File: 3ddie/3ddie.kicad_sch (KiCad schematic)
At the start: 53 parts, among them J1 USB4105-GF-A, J2 TRS_MIDI_IN, J3 TRS_MIDI_OUT, U1 W25Q128JV, U2 RP2040, U3 MCP1702T-3302E_CB, U4 MGC3130-I/MQ, U5 MCP1416R, U6 6N137, U7 BoostedElectrodes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

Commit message: continue adding footprints
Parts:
- C16, C17: footprint Capacitor_SMD:C_0603_1608Metric -> Capacitor_SMD:C_0402_1005Metric
- J2, J3: footprint (none) -> Connector_Audio:Jack_3.5mm_CUI_SJ-3523-SMT_Horizontal; Digikey Catalog # (none) -> CP-3523SJCT-ND; Manufacturer Part # (none) -> SJ-3523-SMT-TR
- U4: footprint (none) -> 3ddie:MGC3130T-I_MQ
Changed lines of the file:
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@@
       (effects (font (size 1.27 1.27)) (justify right))
     )
-    (property "Footprint" "Capacitor_SMD:C_0603_1608Metric" (id 2) (at 259.3848 152.4 0)
+    (property "Footprint" "Capacitor_SMD:C_0402_1005Metric" (id 2) (at 259.3848 152.4 0)
       (effects (font (size 1.27 1.27)) hide)
     )
@@
       (effects (font (size 1.27 1.27)) (justify right))
     )
-    (property "Footprint" "" (id 2) (at 207.645 201.93 0)
-      (effects (font (size 1.27 1.27)) hide)
-    )
-    (property "Datasheet" "~" (id 3) (at 207.645 201.93 0)
+    (property "Footprint" "Connector_Audio:Jack_3.5mm_CUI_SJ-3523-SMT_Horizontal" (id 2) (at 207.645 201.93 0)
+      (effects (font (size 1.27 1.27)) hide)
+    )
+    (property "Datasheet" "https://www.cuidevices.com/product/resource/sj-352x-smt.pdf" (id 3) (at 207.645 201.93 0)
+      (effects (font (size 1.27 1.27)) hide)
+    )
+    (property "Digikey Catalog #" "CP-3523SJCT-ND" (id 4) (at 207.645 201.93 0)
+      (effects (font (size 1.27 1.27)) hide)
+    )
+    (property "Manufacturer Part #" "SJ-3523-SMT-TR" (id 5) (at 207.645 201.93 0)
       (effects (font (size 1.27 1.27)) hide)
     )
@@
     (property "Reference" "J2" (id 0) (at 204.47 172.8302 0))
     (property "Value" "TRS_MIDI_IN" (id 1) (at 204.47 175.3671 0))
-    (property "Footprint" "" (id 2) (at 206.375 180.34 0)
-      (effects (font (size 1.27 1.27)) hide)
-    )
-    (property "Datasheet" "~" (id 3) (at 206.375 180.34 0)
+    (property "Footprint" "Connector_Audio:Jack_3.5mm_CUI_SJ-3523-SMT_Horizontal" (id 2) (at 206.375 180.34 0)
+      (effects (font (size 1.27 1.27)) hide)
+    )
+    (property "Datasheet" "https://www.cuidevices.com/product/resource/sj-352x-smt.pdf" (id 3) (at 206.375 180.34 0)
+      (effects (font (size 1.27 1.27)) hide)
+    )
+    (property "Digikey Catalog #" "CP-3523SJCT-ND" (id 4) (at 206.375 180.34 0)
+      (effects (font (size 1.27 1.27)) hide)
+    )
+    (property "Manufacturer Part #" "SJ-3523-SMT-TR" (id 5) (at 206.375 180.34 0)
       (effects (font (size 1.27 1.27)) hide)
     )
@@
       (effects (font (size 1.524 1.524)) (justify right))
     )
-    (property "Footprint" "" (id 2) (at 223.52 124.714 0)
+    (property "Footprint" "3ddie:MGC3130T-I_MQ" (id 2) (at 223.52 124.714 0)
       (effects (font (size 1.524 1.524)) hide)
     )
@@
       (effects (font (size 1.27 1.27)) (justify right))
     )
-    (property "Footprint" "Capacitor_SMD:C_0603_1608Metric" (id 2) (at 254.3048 152.4 0)
+    (property "Footprint" "Capacitor_SMD:C_0402_1005Metric" (id 2) (at 254.3048 152.4 0)
       (effects (font (size 1.27 1.27)) hide)
     )
@@
       (effects (font (size 1.524 1.524)))
     )
-    (property "Footprint" "" (id 2) (at 251.46 71.374 0)
+    (property "Footprint" "3ddie:MGC3130T-I_MQ" (id 2) (at 251.46 71.374 0)
       (effects (font (size 1.524 1.524)) hide)
     )
@@
     )
     (path "/900c03b9-9a9a-4efc-b87d-5814d26cd06f"
-      (reference "C16") (unit 1) (value "4.7μF") (footprint "Capacitor_SMD:C_0603_1608Metric")
+      (reference "C16") (unit 1) (value "4.7μF") (footprint "Capacitor_SMD:C_0402_1005Metric")
     )
     (path "/1a86f12e-e638-446c-972e-a7709025dbe9"
-      (reference "C17") (unit 1) (value "4.7μF") (footprint "Capacitor_SMD:C_0603_1608Metric")
+      (reference "C17") (unit 1) (value "4.7μF") (footprint "Capacitor_SMD:C_0402_1005Metric")
     )
     (path "/951f6575-df68-4f23-a749-6a530106a298"
@@
     )
     (path "/3f49297e-868a-4cfd-a836-aea36d28a6f3"
-      (reference "J2") (unit 1) (value "TRS_MIDI_IN") (footprint "")
+      (reference "J2") (unit 1) (value "TRS_MIDI_IN") (footprint "Connector_Audio:Jack_3.5mm_CUI_SJ-3523-SMT_Horizontal")
     )
     (path "/36954f5c-ded0-4f77-a0ed-a1fcda0fcb0f"
-      (reference "J3") (unit 1) (value "TRS_MIDI_OUT") (footprint "")
+      (reference "J3") (unit 1) (value "TRS_MIDI_OUT") (footprint "Connector_Audio:Jack_3.5mm_CUI_SJ-3523-SMT_Horizontal")
     )
     (path "/7ca43cf0-22a3-4ee0-a8c6-940bc048e7d1"
@@
     )
     (path "/a9329e99-609f-4c39-a02d-48cc774ada87"
-      (reference "U4") (unit 1) (value "MGC3130-I/MQ") (footprint "")
+      (reference "U4") (unit 1) (value "MGC3130-I/MQ") (footprint "3ddie:MGC3130T-I_MQ")
     )
     (path "/5936d240-6102-4439-994a-788eb8b3c026"
-      (reference "U4") (unit 2) (value "MGC3130-I/MQ") (footprint "")
+      (reference "U4") (unit 2) (value "MGC3130-I/MQ") (footprint "3ddie:MGC3130T-I_MQ")
     )
     (path "/15b2a124-1eb8-4d1a-932b-488f6e69f5b6"

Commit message: finish assigning footprints (other than electrodes)
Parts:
- U6: footprint (none) -> 3ddie:6N137_Leadbend
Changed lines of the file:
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@@
     (property "Reference" "U6" (id 0) (at 235.585 169.0202 0))
     (property "Value" "6N137" (id 1) (at 235.585 171.5571 0))
-    (property "Footprint" "" (id 2) (at 235.585 193.04 0)
+    (property "Footprint" "3ddie:6N137_Leadbend" (id 2) (at 235.585 193.04 0)
       (effects (font (size 1.27 1.27)) hide)
     )
@@
     )
     (path "/bca2ac86-8d9c-4b32-ab1d-2258827622a1"
-      (reference "U6") (unit 1) (value "6N137") (footprint "")
+      (reference "U6") (unit 1) (value "6N137") (footprint "3ddie:6N137_Leadbend")
     )
     (path "/0030390e-c97e-47e6-97d2-f7c983a931fc"

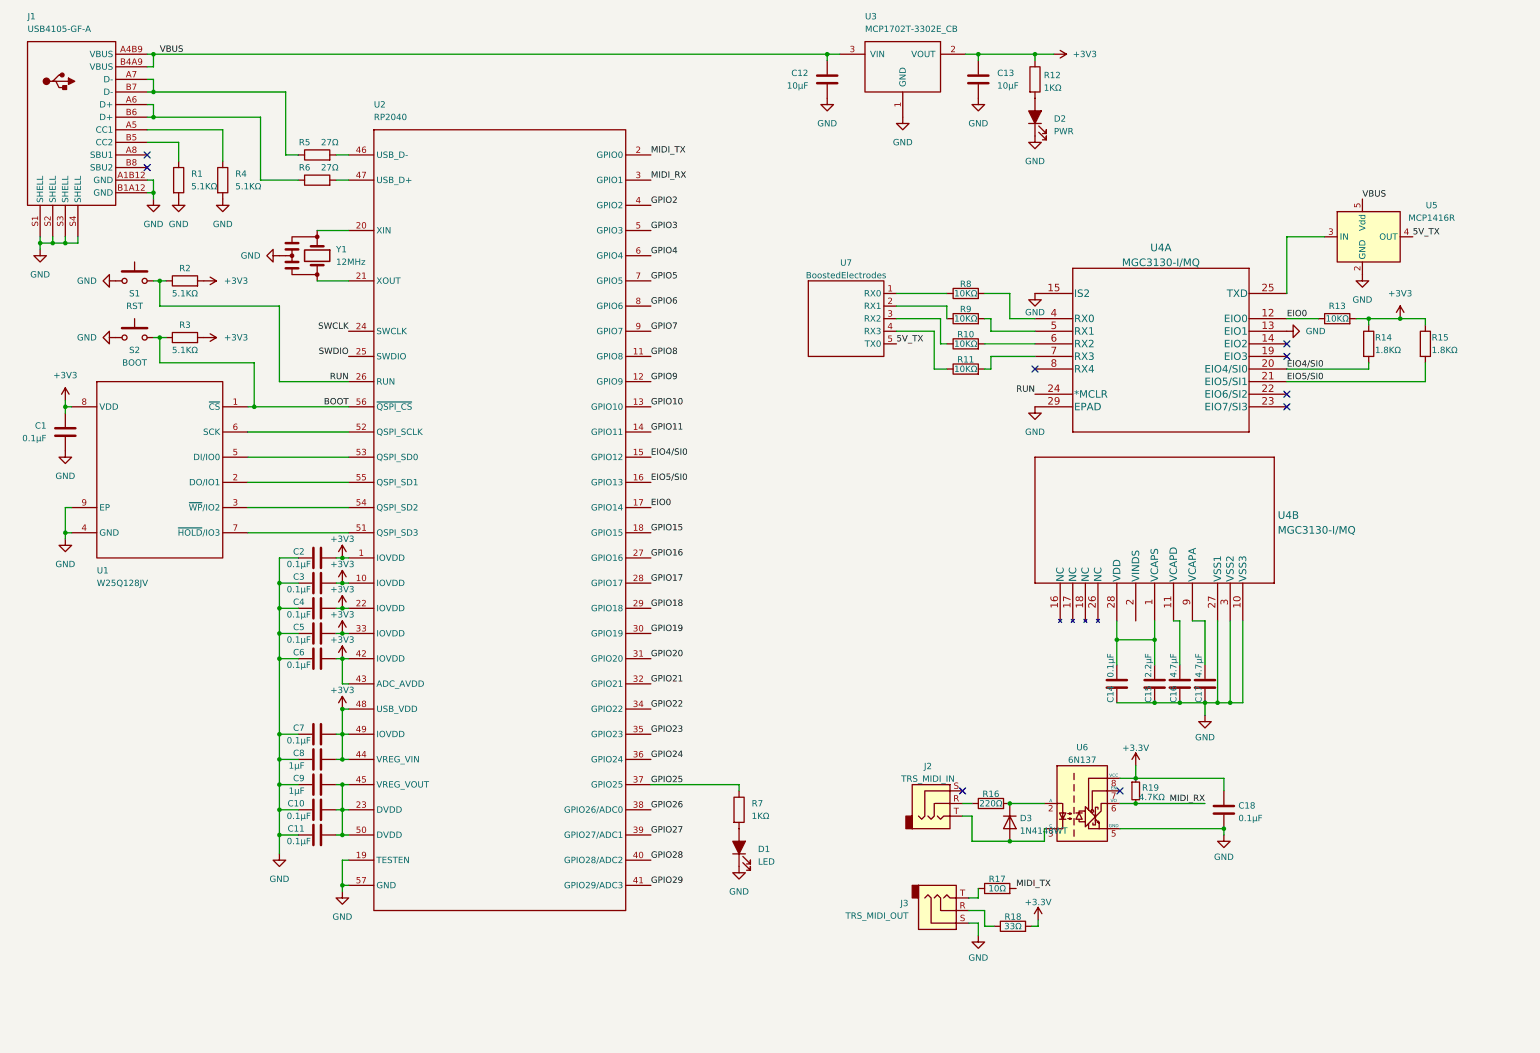
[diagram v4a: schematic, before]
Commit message: add bypass caps to level shifter, start mgc portion of layout
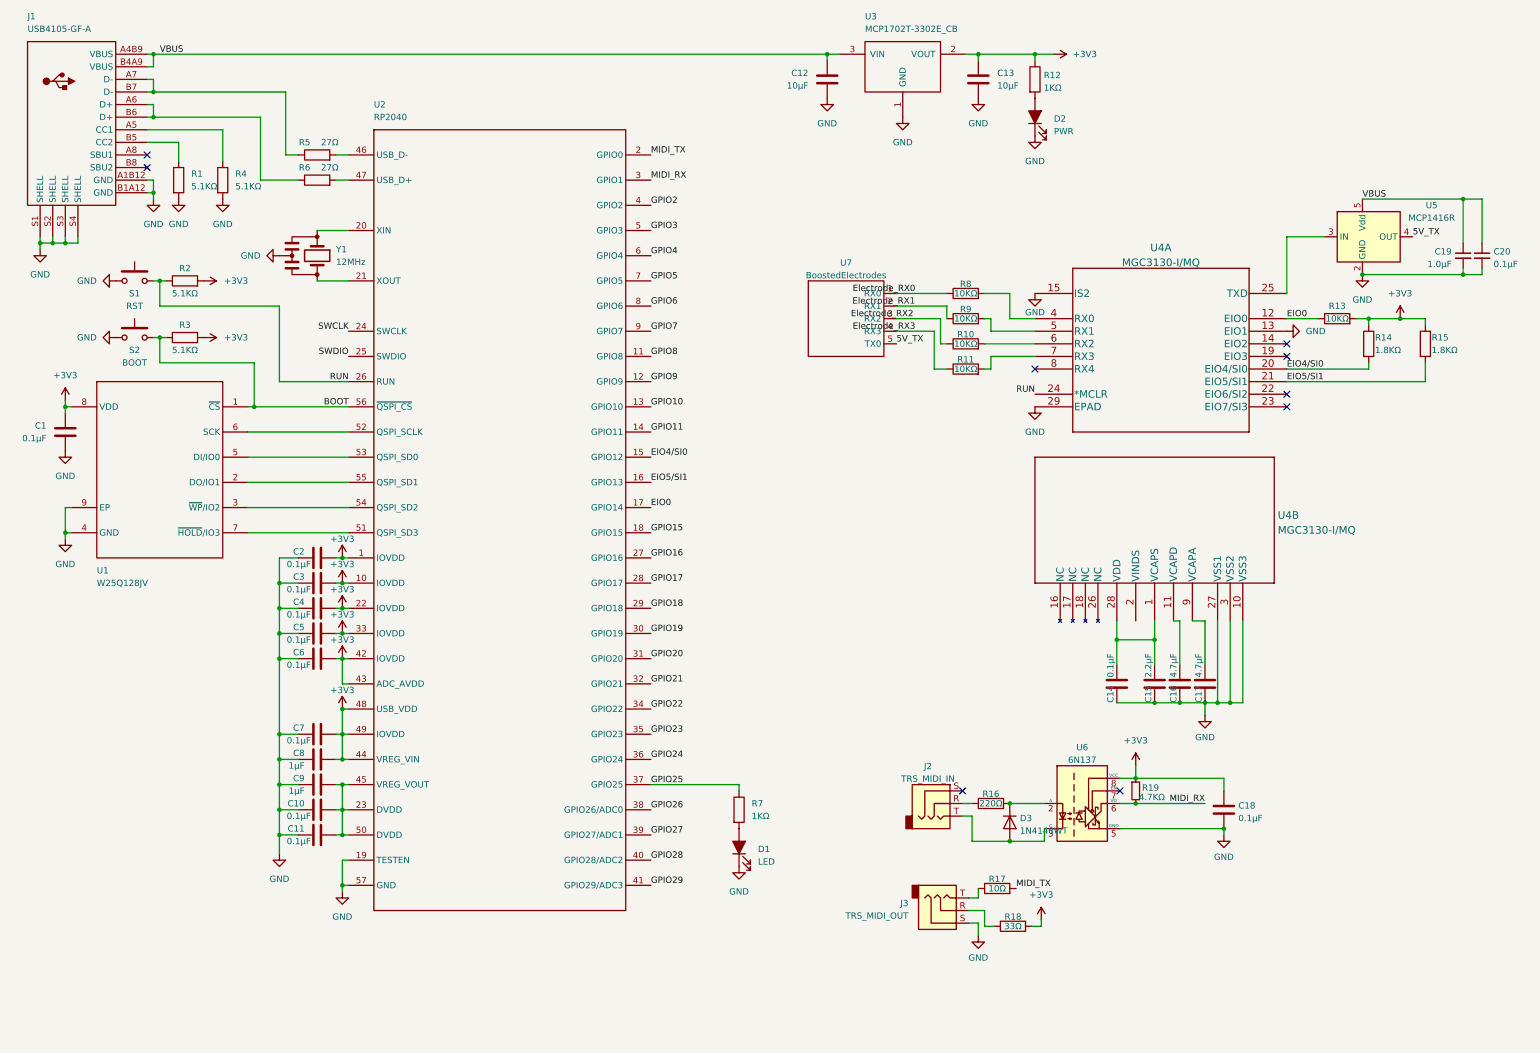
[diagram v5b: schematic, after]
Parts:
- added C19: 1.0μF, Capacitor_SMD:C_0603_1608Metric, symbol Device:C_Small
- added C20: 0.1μF, Capacitor_SMD:C_0603_1608Metric, symbol Device:C_Small
- C1, C10, C11, C14, C15, C16, C17, C18, C2, C3, C4, C5, C6, C7, C8, C9: footprint Capacitor_SMD:C_0402_1005Metric -> Capacitor_SMD:C_0603_1608Metric
- R1, R10, R11, R12, R13, R14, R15, R16, R17, R18, R19, R2, R3, R4, R5, R6, R7, R8, R9: footprint Resistor_SMD:R_0402_1005Metric -> Resistor_SMD:R_0603_1608Metric
- U7: now left out of the parts list
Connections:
- net +3.3V is gone; now on net +3V3: C18.1, R18.2, R19.1, U6.8 (VCC)
- net GND: now also C19.2, C20.2
- net VBUS: now also C19.1, C20.1
- net Electrode_RX0: now reaches R8.1, U7.1 (RX0)
- net Electrode_RX1: now reaches R9.1, U7.2 (RX1)
- net Electrode_RX2: now reaches R10.1, U7.3 (RX2)
- net Electrode_RX3: now reaches R11.1, U7.4 (RX3)
- net EIO5/SI0 renamed EIO5/SI1

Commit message: switch to through hole mounting trs jacks
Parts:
- J2, J3: footprint Connector_Audio:Jack_3.5mm_CUI_SJ-3523-SMT_Horizontal -> Connector_Audio:Jack_3.5mm_CUI_SJ1-3533NG_Horizontal; Digikey Catalog # CP-3523SJCT-ND -> CP1-3533NG-ND; Manufacturer Part # SJ-3523-SMT-TR -> SJ1-3533NG
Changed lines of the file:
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@@
       (effects (font (size 1.27 1.27)) (justify right))
     )
-    (property "Footprint" "Connector_Audio:Jack_3.5mm_CUI_SJ-3523-SMT_Horizontal" (id 2) (at 207.645 201.93 0)
-      (effects (font (size 1.27 1.27)) hide)
-    )
-    (property "Datasheet" "https://www.cuidevices.com/product/resource/sj-352x-smt.pdf" (id 3) (at 207.645 201.93 0)
-      (effects (font (size 1.27 1.27)) hide)
-    )
-    (property "Digikey Catalog #" "CP-3523SJCT-ND" (id 4) (at 207.645 201.93 0)
-      (effects (font (size 1.27 1.27)) hide)
-    )
-    (property "Manufacturer Part #" "SJ-3523-SMT-TR" (id 5) (at 207.645 201.93 0)
+    (property "Footprint" "Connector_Audio:Jack_3.5mm_CUI_SJ1-3533NG_Horizontal" (id 2) (at 207.645 201.93 0)
+      (effects (font (size 1.27 1.27)) hide)
+    )
+    (property "Datasheet" "https://www.cuidevices.com/product/resource/sj1-353xng.pdf" (id 3) (at 207.645 201.93 0)
+      (effects (font (size 1.27 1.27)) hide)
+    )
+    (property "Digikey Catalog #" "CP1-3533NG-ND" (id 4) (at 207.645 201.93 0)
+      (effects (font (size 1.27 1.27)) hide)
+    )
+    (property "Manufacturer Part #" "SJ1-3533NG" (id 5) (at 207.645 201.93 0)
       (effects (font (size 1.27 1.27)) hide)
     )
@@
     (property "Reference" "J2" (id 0) (at 204.47 172.8302 0))
     (property "Value" "TRS_MIDI_IN" (id 1) (at 204.47 175.3671 0))
-    (property "Footprint" "Connector_Audio:Jack_3.5mm_CUI_SJ-3523-SMT_Horizontal" (id 2) (at 206.375 180.34 0)
-      (effects (font (size 1.27 1.27)) hide)
-    )
-    (property "Datasheet" "https://www.cuidevices.com/product/resource/sj-352x-smt.pdf" (id 3) (at 206.375 180.34 0)
-      (effects (font (size 1.27 1.27)) hide)
-    )
-    (property "Digikey Catalog #" "CP-3523SJCT-ND" (id 4) (at 206.375 180.34 0)
-      (effects (font (size 1.27 1.27)) hide)
-    )
-    (property "Manufacturer Part #" "SJ-3523-SMT-TR" (id 5) (at 206.375 180.34 0)
+    (property "Footprint" "Connector_Audio:Jack_3.5mm_CUI_SJ1-3533NG_Horizontal" (id 2) (at 206.375 180.34 0)
+      (effects (font (size 1.27 1.27)) hide)
+    )
+    (property "Datasheet" "https://www.cuidevices.com/product/resource/sj1-353xng.pdf" (id 3) (at 206.375 180.34 0)
+      (effects (font (size 1.27 1.27)) hide)
+    )
+    (property "Digikey Catalog #" "CP1-3533NG-ND" (id 4) (at 206.375 180.34 0)
+      (effects (font (size 1.27 1.27)) hide)
+    )
+    (property "Manufacturer Part #" "SJ1-3533NG" (id 5) (at 206.375 180.34 0)
       (effects (font (size 1.27 1.27)) hide)
     )
@@
     )
     (path "/3f49297e-868a-4cfd-a836-aea36d28a6f3"
-      (reference "J2") (unit 1) (value "TRS_MIDI_IN") (footprint "Connector_Audio:Jack_3.5mm_CUI_SJ-3523-SMT_Horizontal")
+      (reference "J2") (unit 1) (value "TRS_MIDI_IN") (footprint "Connector_Audio:Jack_3.5mm_CUI_SJ1-3533NG_Horizontal")
     )
     (path "/36954f5c-ded0-4f77-a0ed-a1fcda0fcb0f"
-      (reference "J3") (unit 1) (value "TRS_MIDI_OUT") (footprint "Connector_Audio:Jack_3.5mm_CUI_SJ-3523-SMT_Horizontal")
+      (reference "J3") (unit 1) (value "TRS_MIDI_OUT") (footprint "Connector_Audio:Jack_3.5mm_CUI_SJ1-3533NG_Horizontal")
     )
     (path "/7ca43cf0-22a3-4ee0-a8c6-940bc048e7d1"
